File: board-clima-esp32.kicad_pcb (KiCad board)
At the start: 2 copper layers, 77.7 x 64.3 mm, 56 parts, among them IC1 ESP32-S3-WROOM-1-N4, J1 Conn_01x06_Pin, J2 Screw_Terminal_01x03, J3 Conn_01x04_Pin, J5 Conn_01x05_Pin, J6 USB_C_Receptacle, Q1 AO3400A, Q2 AO3401A, Q3 AO3400A, SW1 RESET, SW2 BOOT, U1 AMS1117-3.3, U3 PC817, U4 PC817

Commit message: silkscreen
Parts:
- D10, D8, D9: footprint Diode_SMD:D_SOD-323 -> Diode_SMD:D_SOD-123
- moved D9 0.76 mm to (156.5, 173.2)
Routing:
- net Net-(D10-K): track 21.2 -> 17.8 mm
- net /OT_COM: track 48.8 -> 45.9 mm
- net /OT_HIGH: track 10.7 -> 12.1 mm
- net Net-(D9-K): track 6.90 -> 6.33 mm
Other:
- outline, holes or cut-outs redrawn
- board text added: "JLCJLCJLCJLC"

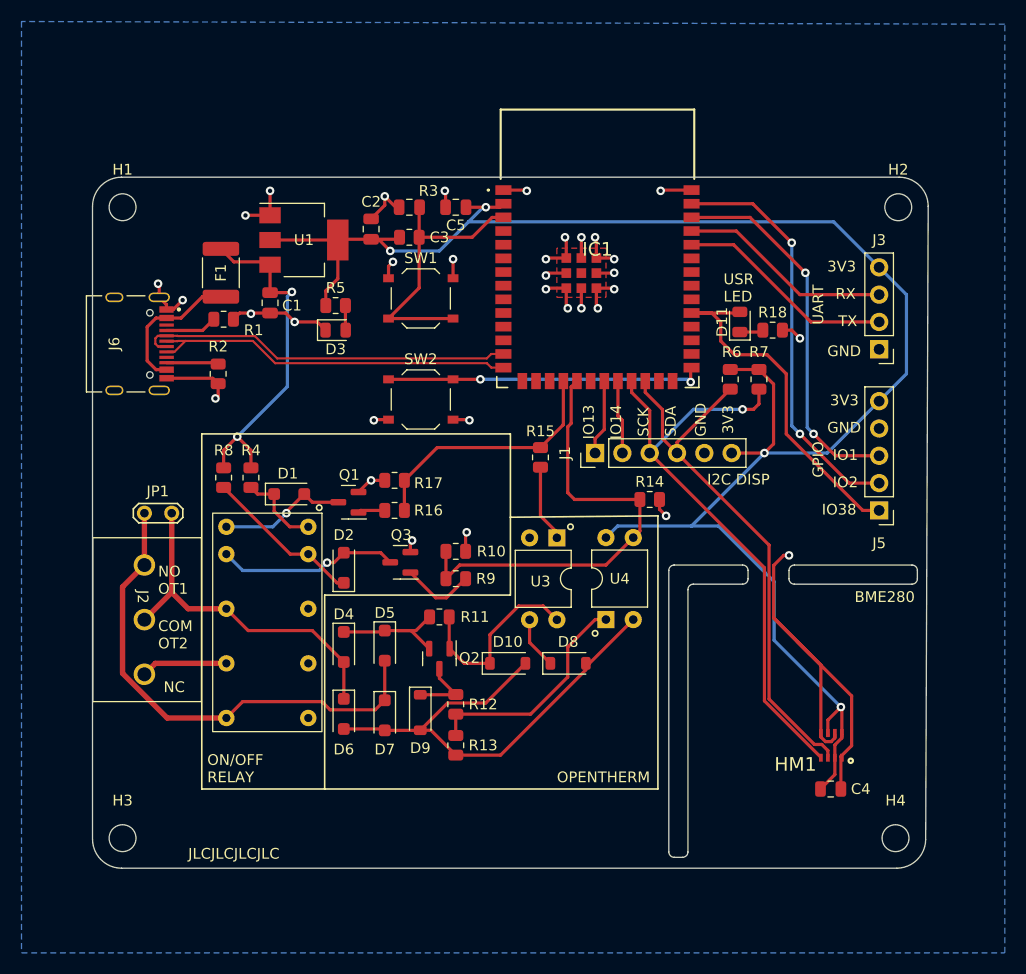
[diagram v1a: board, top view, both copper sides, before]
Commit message: new PWR connector, front copper pour
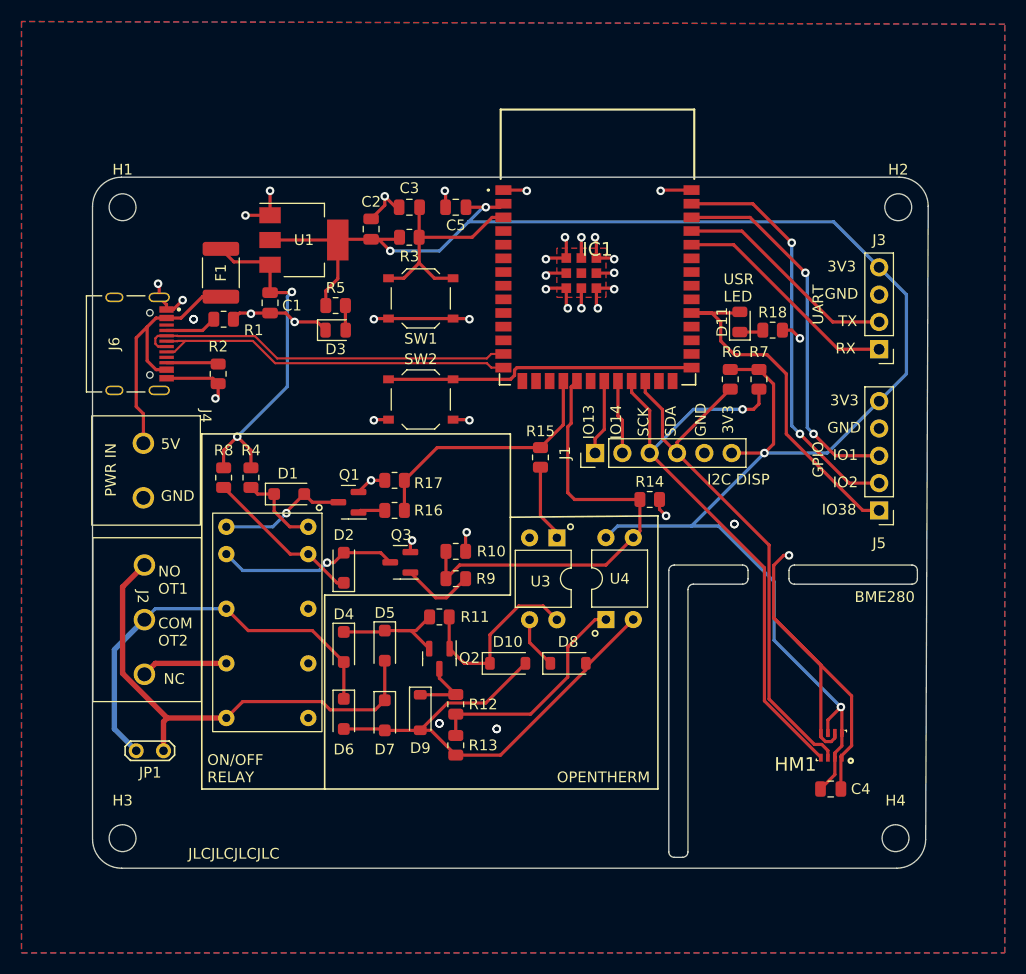
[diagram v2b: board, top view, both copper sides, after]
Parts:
- added J4: Screw_Terminal_01x02, XYEK500-5.08-3P:XYEK500-5.08-2P, F.Cu at (136.0, 145.6)
- moved JP1 22.3 mm to (130.0, 176.8), turned to 0 degrees
- turned SW1 to 180 degrees
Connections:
- net Net-(F1-Pad1) renamed /5VIN
- J3 pad 1: GND -> /UART_RX
- J3 pad 2: /UART_RX -> /UART_TX
- J3 pad 3: /UART_TX -> GND
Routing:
- net /5VIN: track 13.3 -> 24.8 mm
- net /R_COM: track 33.1 -> 38.6 mm
- net GND: track 117.3 -> 122.8 mm, vias 33 -> 41
- net Net-(IC1-EN): track 26.1 -> 21.0 mm
- net /R_NO: track 46.8 -> 45.2 mm
- net /UART_RX: track 20.4 -> 21.5 mm
- net /UART_TX: track 19.9 -> 20.9 mm
- net /BOOT: track 29.6 -> 28.9 mm, vias 2 -> 0
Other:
- board text added: "5V"
- board text added: "BOILER"
- board text added: "PWR IN"

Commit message: final corrections
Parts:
- added IO10 B1: TestPoint, TestPoint:TestPoint_Pad_D1.0mm, F.Cu at (160.3, 151.6)
- added IO11 B2: TestPoint, TestPoint:TestPoint_Pad_D1.0mm, F.Cu at (160.3, 154.7)
- added TP3: TestPoint, TestPoint:TestPoint_Pad_D1.0mm, B.Cu at (184.9, 136.7)
- added TP4: TestPoint, TestPoint:TestPoint_Pad_D1.0mm, B.Cu at (184.9, 134.6)
- added TP5: TestPoint, TestPoint:TestPoint_Pad_D1.0mm, B.Cu at (184.9, 132.3)
- added TP6: TestPoint, TestPoint:TestPoint_Pad_D1.0mm, B.Cu at (184.9, 130.3)
- moved H1 1.08 mm to (129.5, 127.0)
- moved H2 1.08 mm to (200.2, 127.0)
- moved H3 1.08 mm to (129.5, 184.2)
- moved H4 1.08 mm to (199.9, 184.2)
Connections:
- IC1 pad 32: unconnected-(IC1-IO39-Pad32) -> Net-(IC1-IO39)
- IC1 pad 33: unconnected-(IC1-IO40-Pad33) -> Net-(IC1-IO40)
- IC1 pad 34: unconnected-(IC1-IO41-Pad34) -> Net-(IC1-IO41)
- IC1 pad 35: unconnected-(IC1-IO42-Pad35) -> Net-(IC1-IO42)
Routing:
- net /R_COM: track 38.6 -> 24.4 mm
- net Net-(D2-K): track 14.8 -> 21.0 mm
- net /BOILER_2: track 43.0 -> 47.2 mm
- net Net-(IC1-IO39): track 0.00 -> 4.13 mm, vias 0 -> 1
- net /BOILER_1: track 23.8 -> 27.7 mm
- net Net-(IC1-IO40): track 0.00 -> 3.67 mm, vias 0 -> 1
- net Net-(IC1-IO42): track 0.00 -> 3.51 mm, vias 0 -> 1
- net Net-(IC1-IO41): track 0.00 -> 3.25 mm, vias 0 -> 1
- net /R_NO: track 45.2 -> 47.6 mm
- net GND: vias 41 -> 43
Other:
- board text added: "BOARD VARIANT [ ] RELAY [ ] OPENTHERM [ ] BME280 DON'T MOUNT BOTH RELAY AND OT AT THE SAME TIME!"
- board text added: "BYPASS"
- board text added: "EMERG JTAG"
- board text removed: "BOARD VARIANT [ ] RELAY [ ] OPENTHERM [ ] BME280 RELAY/OPENTHERM VARIANTS ARE MUTUALLY EXCLUSIVE DON'T MOUNT BOTH AT THE SAME TIME!"

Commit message: drc pass
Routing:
- net /R_COM: track 24.4 -> 37.7 mm
- net GND: vias 43 -> 38

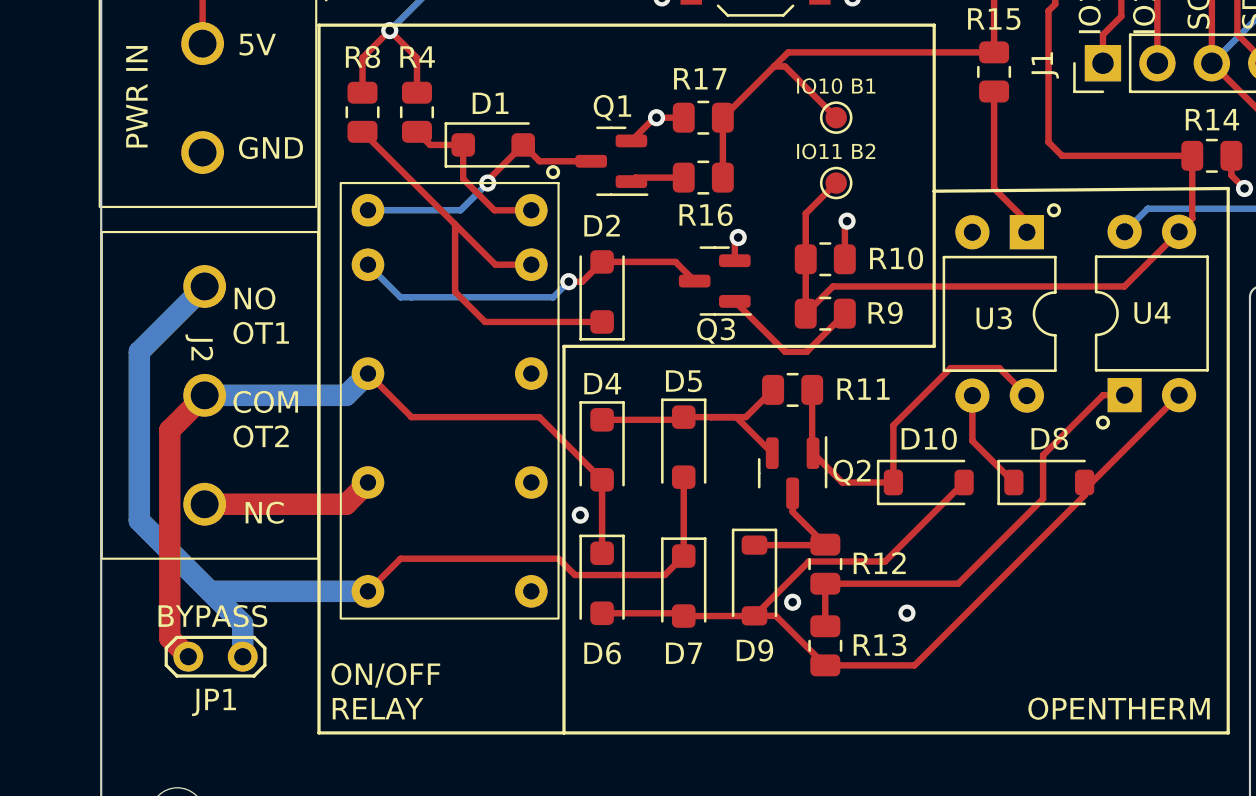
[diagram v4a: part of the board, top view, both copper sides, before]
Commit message: flipped relay
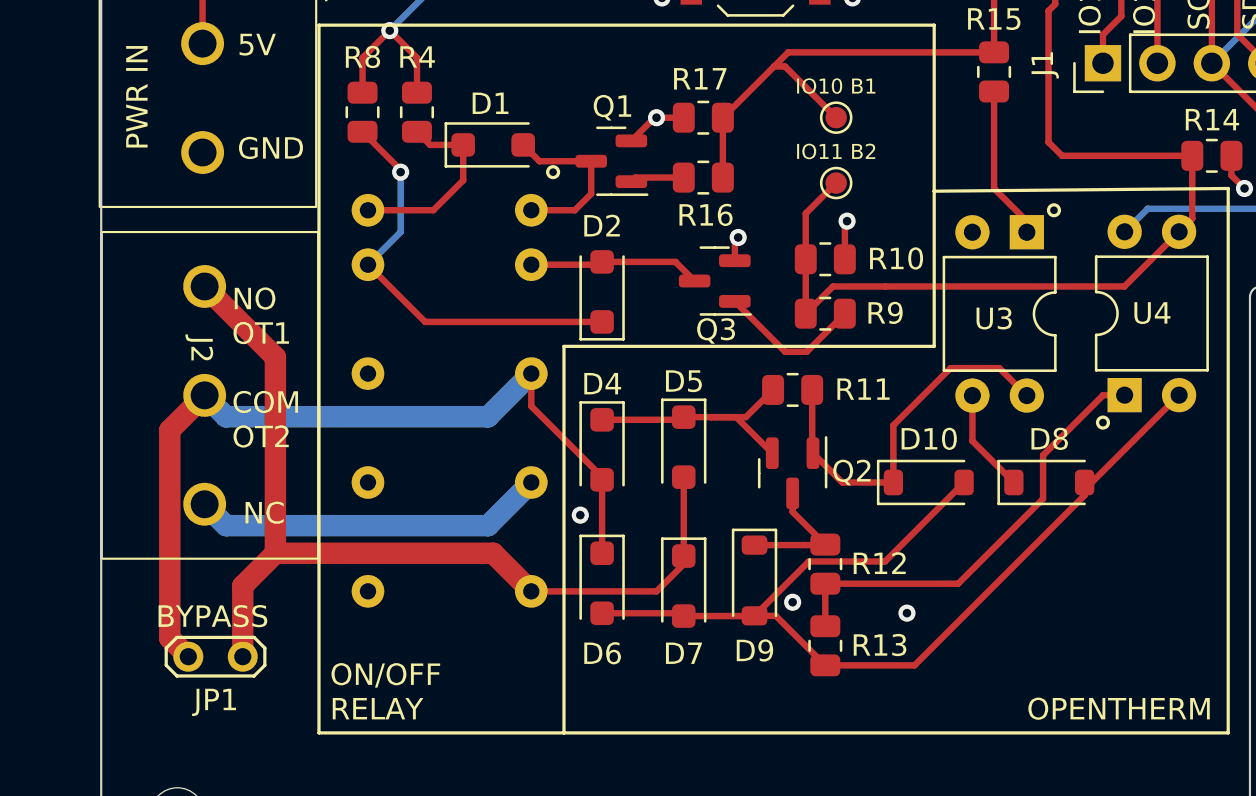
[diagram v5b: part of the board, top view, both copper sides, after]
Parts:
- U2: moved to B.Cu
- moved U2 10.2 mm to (137.2, 154.7)
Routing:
- net Net-(D2-A): track 16.9 -> 8.04 mm, vias 1 -> 0
- net /R_NC: track 8.04 -> 16.5 mm
- net /R_NO: track 47.6 -> 43.6 mm
- net Net-(D1-A): track 12.1 -> 8.12 mm, vias 1 -> 0
- net /R_COM: track 37.7 -> 39.5 mm
- net Net-(D2-K): track 21.0 -> 19.6 mm, vias 0 -> 1
- net Net-(D1-K): track 7.78 -> 9.08 mm

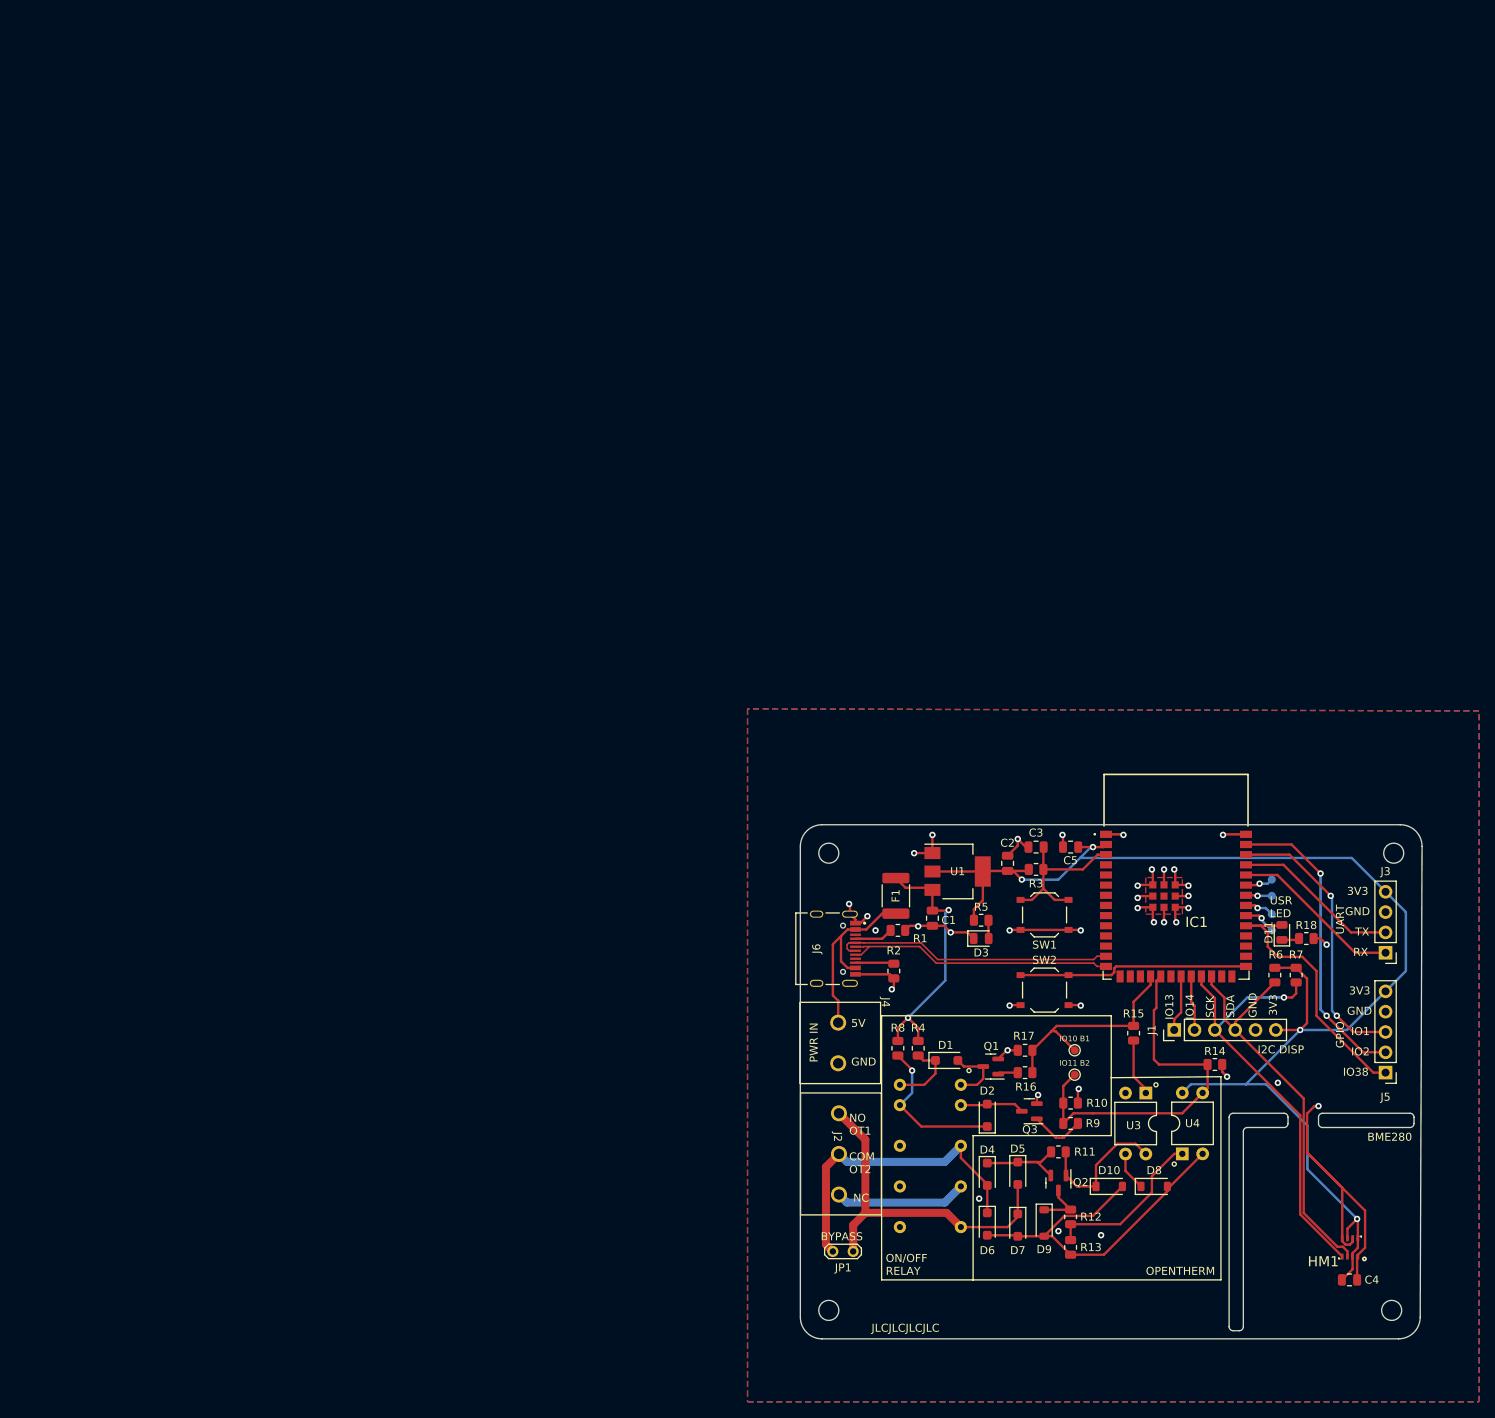
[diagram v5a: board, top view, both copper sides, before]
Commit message: relay was flipped :(
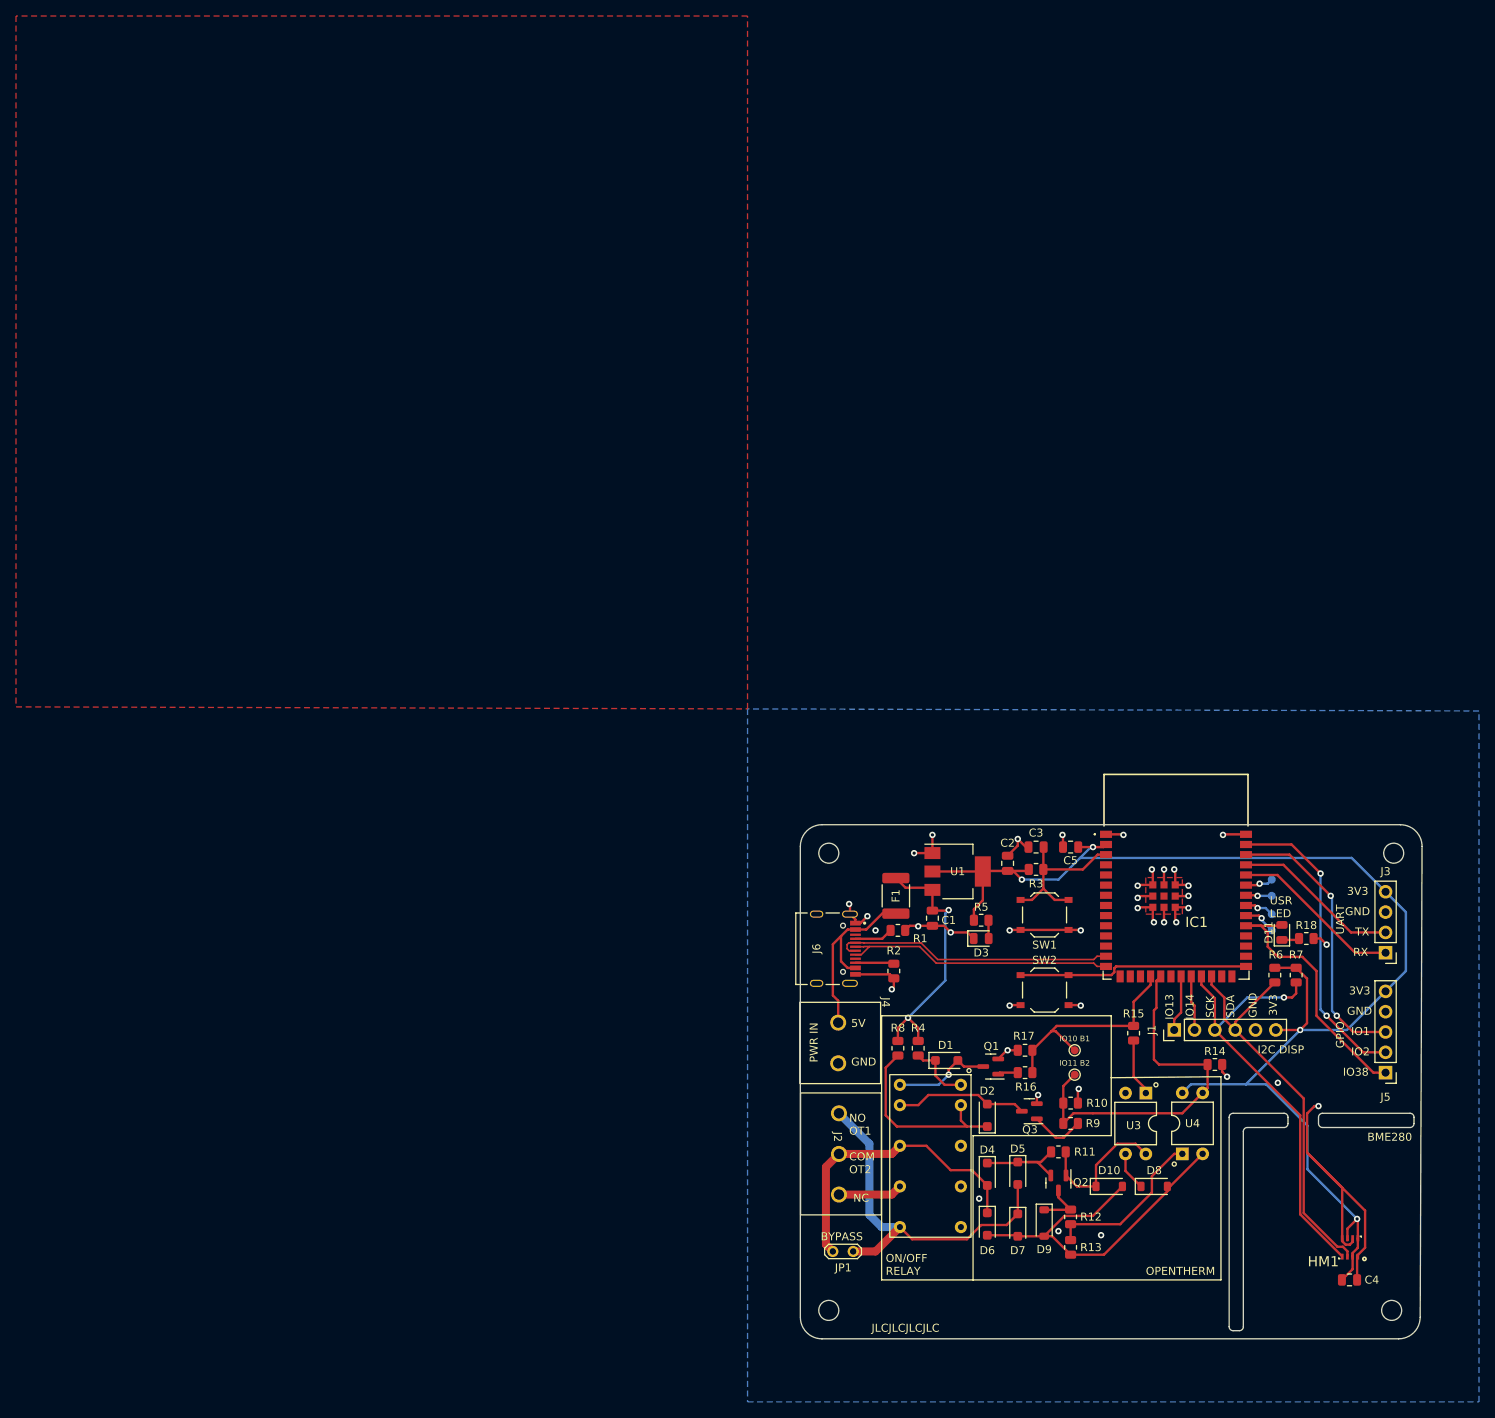
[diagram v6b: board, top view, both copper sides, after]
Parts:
- U2: moved to F.Cu
- moved U2 10.2 mm to (147.3, 154.7)
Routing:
- net Net-(D2-A): track 8.04 -> 16.6 mm
- net /R_NC: track 16.5 -> 8.04 mm
- net Net-(D2-K): track 19.6 -> 24.4 mm, vias 1 -> 0
- net Net-(D1-A): track 8.12 -> 12.4 mm, vias 0 -> 1
- net /R_NO: track 43.6 -> 46.2 mm
- net /R_COM: track 39.5 -> 37.7 mm
- net Net-(D1-K): track 9.08 -> 7.96 mm
